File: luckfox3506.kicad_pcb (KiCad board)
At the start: 2 copper layers, 29.7 x 29.2 mm, 1 part

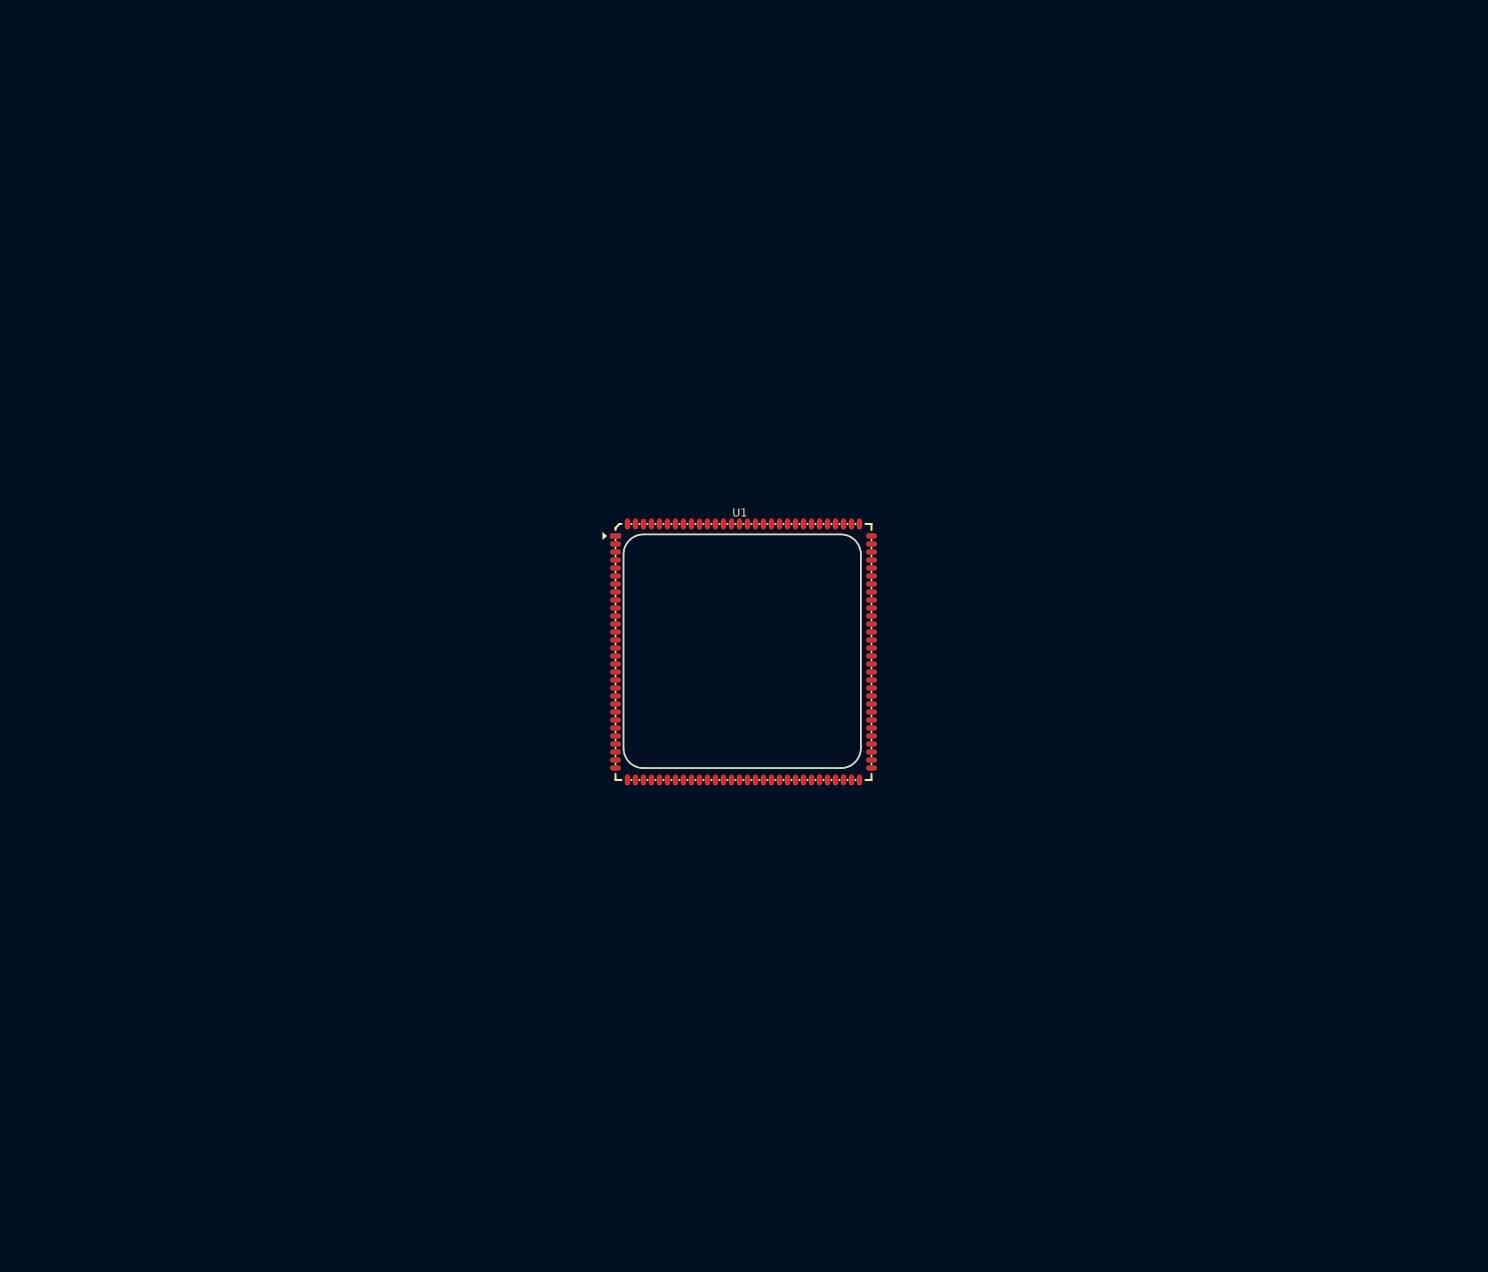
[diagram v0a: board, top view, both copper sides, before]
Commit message: Added footprints for headers
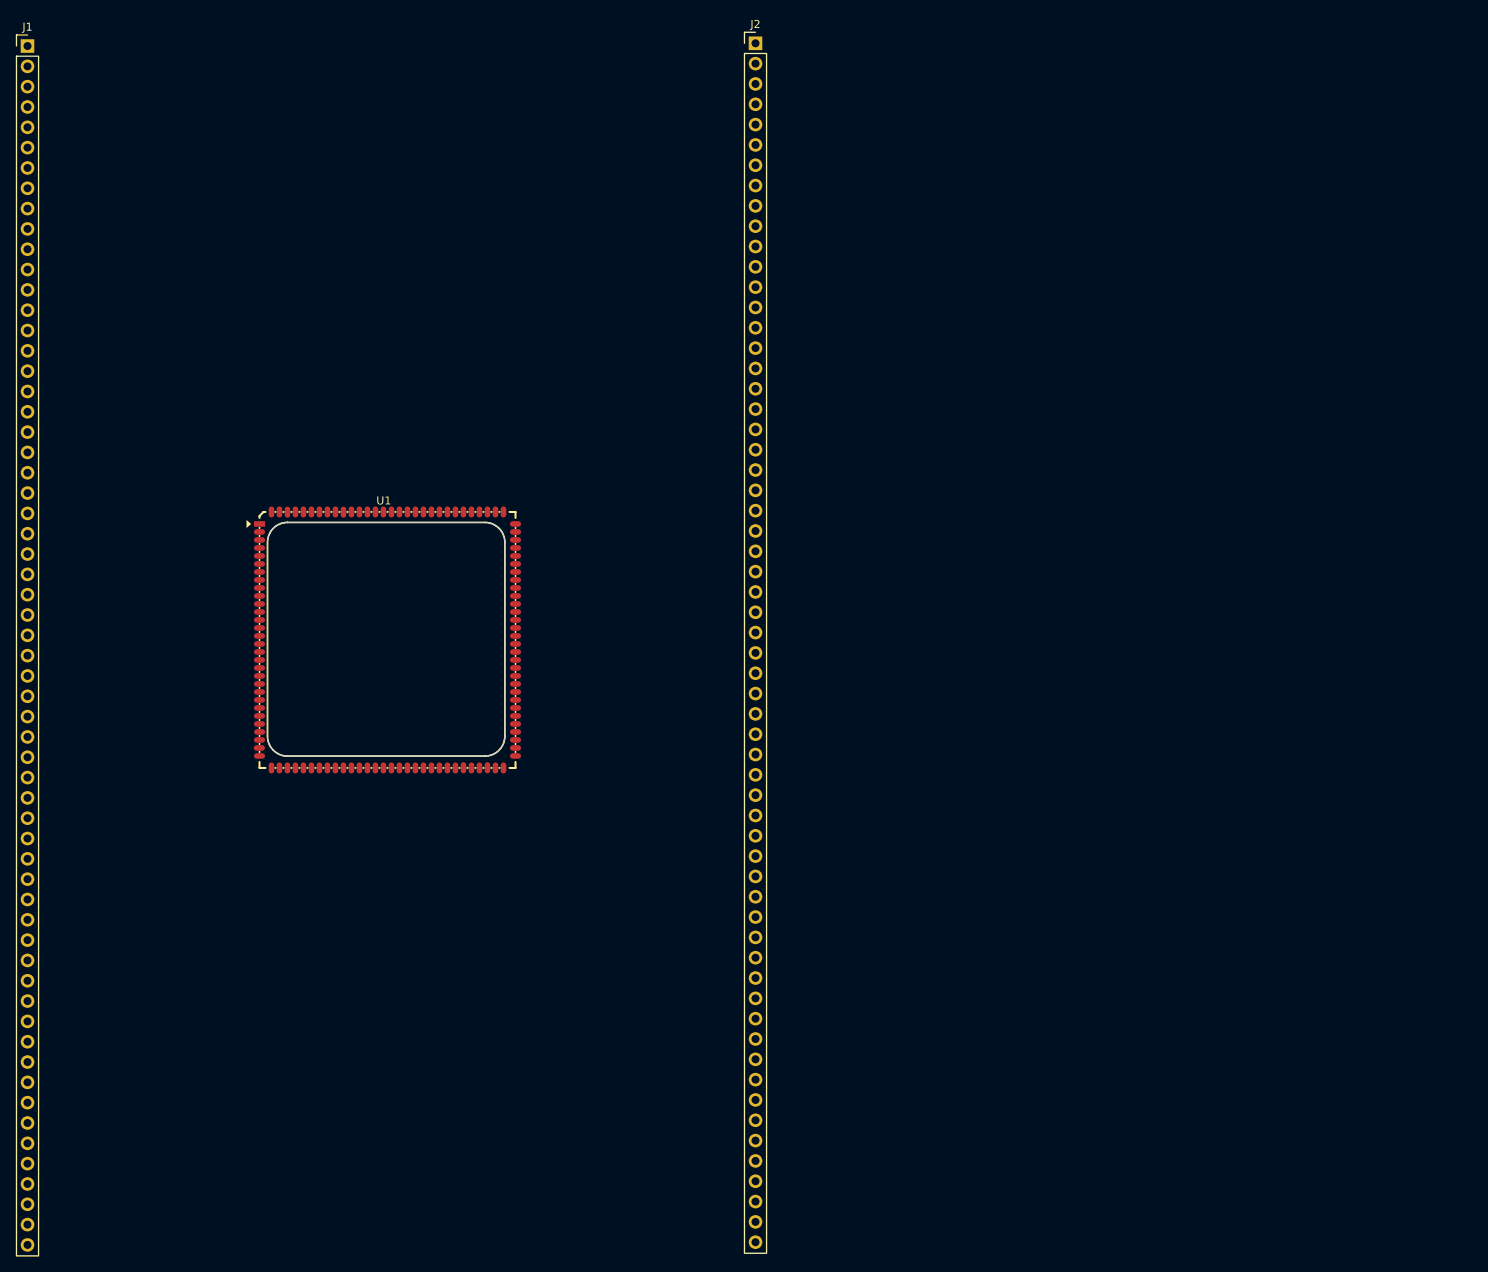
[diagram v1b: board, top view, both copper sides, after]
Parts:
- added J1: Conn_01x60, Library:PinHeader_1x60_P2.54mm_Vertical, F.Cu at (60.5, 25.3)
- added J2: Conn_01x60, Library:PinHeader_1x60_P2.54mm_Vertical, F.Cu at (151.5, 24.9)
- moved U1 44.5 mm to (105.5, 99.5)

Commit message: Added nets
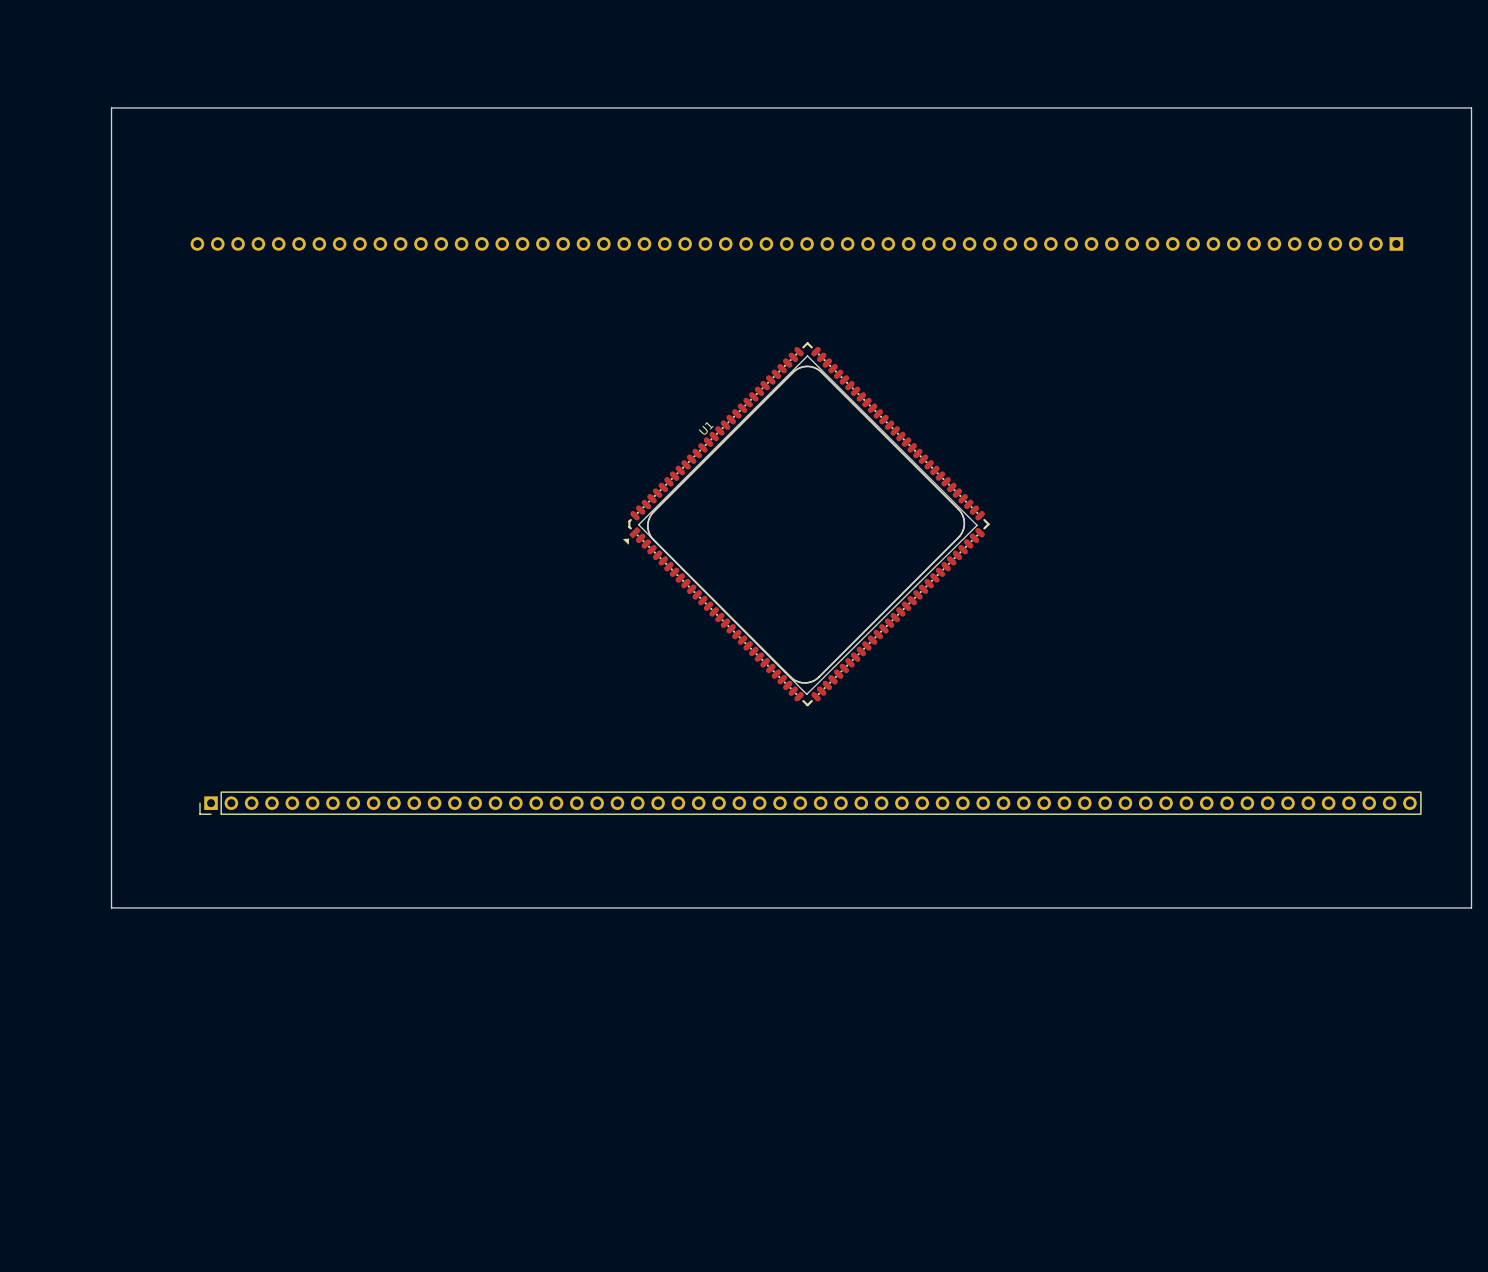
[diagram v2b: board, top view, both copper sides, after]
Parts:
- J2: moved to B.Cu
- U1: footprint Core3506:CORE3506_[32_32]_120P -> custom:CORE3506_[32_32]_120P
- moved J1 97.4 mm to (83.4, 119.9), turned to 90 degrees
- moved J2 83.9 mm to (231.6, 50.0), turned to 90 degrees
- moved U1 54.5 mm to (158.0, 85.0), turned to 45 degrees
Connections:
- J1 pad 1: unconnected-(J1-Pin_1-Pad1) -> Net-(J1-Pin_1)
- J1 pad 10: unconnected-(J1-Pin_10-Pad10) -> Net-(J1-Pin_10)
- J1 pad 11: unconnected-(J1-Pin_11-Pad11) -> Net-(J1-Pin_11)
- J1 pad 12: unconnected-(J1-Pin_12-Pad12) -> Net-(J1-Pin_12)
- J1 pad 13: unconnected-(J1-Pin_13-Pad13) -> Net-(J1-Pin_13)
- J1 pad 14: unconnected-(J1-Pin_14-Pad14) -> Net-(J1-Pin_14)
- J1 pad 15: unconnected-(J1-Pin_15-Pad15) -> Net-(J1-Pin_15)
- J1 pad 16: unconnected-(J1-Pin_16-Pad16) -> Net-(J1-Pin_16)
- J1 pad 17: unconnected-(J1-Pin_17-Pad17) -> Net-(J1-Pin_17)
- J1 pad 18: unconnected-(J1-Pin_18-Pad18) -> Net-(J1-Pin_18)
- J1 pad 19: unconnected-(J1-Pin_19-Pad19) -> Net-(J1-Pin_19)
- J1 pad 2: unconnected-(J1-Pin_2-Pad2) -> Net-(J1-Pin_2)
- J1 pad 20: unconnected-(J1-Pin_20-Pad20) -> Net-(J1-Pin_20)
- J1 pad 21: unconnected-(J1-Pin_21-Pad21) -> Net-(J1-Pin_21)
- J1 pad 22: unconnected-(J1-Pin_22-Pad22) -> Net-(J1-Pin_22)
- J1 pad 23: unconnected-(J1-Pin_23-Pad23) -> Net-(J1-Pin_23)
- J1 pad 24: unconnected-(J1-Pin_24-Pad24) -> Net-(J1-Pin_24)
- J1 pad 25: unconnected-(J1-Pin_25-Pad25) -> Net-(J1-Pin_25)
- J1 pad 26: unconnected-(J1-Pin_26-Pad26) -> Net-(J1-Pin_26)
- J1 pad 27: unconnected-(J1-Pin_27-Pad27) -> Net-(J1-Pin_27)
- J1 pad 28: unconnected-(J1-Pin_28-Pad28) -> Net-(J1-Pin_28)
- J1 pad 29: unconnected-(J1-Pin_29-Pad29) -> Net-(J1-Pin_29)
- J1 pad 3: unconnected-(J1-Pin_3-Pad3) -> Net-(J1-Pin_3)
- J1 pad 30: unconnected-(J1-Pin_30-Pad30) -> Net-(J1-Pin_30)
- J1 pad 31: unconnected-(J1-Pin_31-Pad31) -> Net-(J1-Pin_31)
- J1 pad 32: unconnected-(J1-Pin_32-Pad32) -> Net-(J1-Pin_32)
- J1 pad 33: unconnected-(J1-Pin_33-Pad33) -> Net-(J1-Pin_33)
- J1 pad 34: unconnected-(J1-Pin_34-Pad34) -> Net-(J1-Pin_34)
- J1 pad 35: unconnected-(J1-Pin_35-Pad35) -> Net-(J1-Pin_35)
- J1 pad 36: unconnected-(J1-Pin_36-Pad36) -> Net-(J1-Pin_36)
- J1 pad 37: unconnected-(J1-Pin_37-Pad37) -> Net-(J1-Pin_37)
- J1 pad 38: unconnected-(J1-Pin_38-Pad38) -> Net-(J1-Pin_38)
- J1 pad 39: unconnected-(J1-Pin_39-Pad39) -> Net-(J1-Pin_39)
- J1 pad 4: unconnected-(J1-Pin_4-Pad4) -> Net-(J1-Pin_4)
- J1 pad 40: unconnected-(J1-Pin_40-Pad40) -> Net-(J1-Pin_40)
- J1 pad 41: unconnected-(J1-Pin_41-Pad41) -> Net-(J1-Pin_41)
- J1 pad 42: unconnected-(J1-Pin_42-Pad42) -> Net-(J1-Pin_42)
- J1 pad 43: unconnected-(J1-Pin_43-Pad43) -> Net-(J1-Pin_43)
- J1 pad 44: unconnected-(J1-Pin_44-Pad44) -> Net-(J1-Pin_44)
- J1 pad 45: unconnected-(J1-Pin_45-Pad45) -> Net-(J1-Pin_45)
- J1 pad 46: unconnected-(J1-Pin_46-Pad46) -> Net-(J1-Pin_46)
- J1 pad 47: unconnected-(J1-Pin_47-Pad47) -> Net-(J1-Pin_47)
- J1 pad 48: unconnected-(J1-Pin_48-Pad48) -> Net-(J1-Pin_48)
- J1 pad 49: unconnected-(J1-Pin_49-Pad49) -> Net-(J1-Pin_49)
- J1 pad 5: unconnected-(J1-Pin_5-Pad5) -> Net-(J1-Pin_5)
- J1 pad 50: unconnected-(J1-Pin_50-Pad50) -> Net-(J1-Pin_50)
- J1 pad 51: unconnected-(J1-Pin_51-Pad51) -> Net-(J1-Pin_51)
- J1 pad 52: unconnected-(J1-Pin_52-Pad52) -> Net-(J1-Pin_52)
- J1 pad 53: unconnected-(J1-Pin_53-Pad53) -> Net-(J1-Pin_53)
- J1 pad 54: unconnected-(J1-Pin_54-Pad54) -> Net-(J1-Pin_54)
- J1 pad 55: unconnected-(J1-Pin_55-Pad55) -> Net-(J1-Pin_55)
- J1 pad 56: unconnected-(J1-Pin_56-Pad56) -> Net-(J1-Pin_56)
- J1 pad 57: unconnected-(J1-Pin_57-Pad57) -> Net-(J1-Pin_57)
- J1 pad 58: unconnected-(J1-Pin_58-Pad58) -> Net-(J1-Pin_58)
- J1 pad 59: unconnected-(J1-Pin_59-Pad59) -> Net-(J1-Pin_59)
- J1 pad 6: unconnected-(J1-Pin_6-Pad6) -> Net-(J1-Pin_6)
- J1 pad 60: unconnected-(J1-Pin_60-Pad60) -> Net-(J1-Pin_60)
- J1 pad 7: unconnected-(J1-Pin_7-Pad7) -> Net-(J1-Pin_7)
- J1 pad 8: unconnected-(J1-Pin_8-Pad8) -> Net-(J1-Pin_8)
- J1 pad 9: unconnected-(J1-Pin_9-Pad9) -> Net-(J1-Pin_9)
- J2 pad 1: unconnected-(J2-Pin_1-Pad1) -> Net-(J2-Pin_1)
- J2 pad 10: unconnected-(J2-Pin_10-Pad10) -> Net-(J2-Pin_10)
- J2 pad 11: unconnected-(J2-Pin_11-Pad11) -> Net-(J2-Pin_11)
- J2 pad 12: unconnected-(J2-Pin_12-Pad12) -> Net-(J2-Pin_12)
- J2 pad 13: unconnected-(J2-Pin_13-Pad13) -> Net-(J2-Pin_13)
- J2 pad 14: unconnected-(J2-Pin_14-Pad14) -> Net-(J2-Pin_14)
- J2 pad 15: unconnected-(J2-Pin_15-Pad15) -> Net-(J2-Pin_15)
- J2 pad 16: unconnected-(J2-Pin_16-Pad16) -> Net-(J2-Pin_16)
- J2 pad 17: unconnected-(J2-Pin_17-Pad17) -> Net-(J2-Pin_17)
- J2 pad 18: unconnected-(J2-Pin_18-Pad18) -> Net-(J2-Pin_18)
- J2 pad 19: unconnected-(J2-Pin_19-Pad19) -> Net-(J2-Pin_19)
- J2 pad 2: unconnected-(J2-Pin_2-Pad2) -> Net-(J2-Pin_2)
- J2 pad 20: unconnected-(J2-Pin_20-Pad20) -> Net-(J2-Pin_20)
- J2 pad 21: unconnected-(J2-Pin_21-Pad21) -> Net-(J2-Pin_21)
- J2 pad 22: unconnected-(J2-Pin_22-Pad22) -> Net-(J2-Pin_22)
- J2 pad 23: unconnected-(J2-Pin_23-Pad23) -> Net-(J2-Pin_23)
- J2 pad 24: unconnected-(J2-Pin_24-Pad24) -> Net-(J2-Pin_24)
- J2 pad 25: unconnected-(J2-Pin_25-Pad25) -> Net-(J2-Pin_25)
- J2 pad 26: unconnected-(J2-Pin_26-Pad26) -> Net-(J2-Pin_26)
- J2 pad 27: unconnected-(J2-Pin_27-Pad27) -> Net-(J2-Pin_27)
- J2 pad 28: unconnected-(J2-Pin_28-Pad28) -> Net-(J2-Pin_28)
- J2 pad 29: unconnected-(J2-Pin_29-Pad29) -> Net-(J2-Pin_29)
- J2 pad 3: unconnected-(J2-Pin_3-Pad3) -> Net-(J2-Pin_3)
- J2 pad 30: unconnected-(J2-Pin_30-Pad30) -> Net-(J2-Pin_30)
- J2 pad 31: unconnected-(J2-Pin_31-Pad31) -> Net-(J2-Pin_31)
- J2 pad 32: unconnected-(J2-Pin_32-Pad32) -> Net-(J2-Pin_32)
- J2 pad 33: unconnected-(J2-Pin_33-Pad33) -> Net-(J2-Pin_33)
- J2 pad 34: unconnected-(J2-Pin_34-Pad34) -> Net-(J2-Pin_34)
- J2 pad 35: unconnected-(J2-Pin_35-Pad35) -> Net-(J2-Pin_35)
- J2 pad 36: unconnected-(J2-Pin_36-Pad36) -> Net-(J2-Pin_36)
- J2 pad 37: unconnected-(J2-Pin_37-Pad37) -> Net-(J2-Pin_37)
- J2 pad 38: unconnected-(J2-Pin_38-Pad38) -> Net-(J2-Pin_38)
- J2 pad 39: unconnected-(J2-Pin_39-Pad39) -> Net-(J2-Pin_39)
- J2 pad 4: unconnected-(J2-Pin_4-Pad4) -> Net-(J2-Pin_4)
- J2 pad 40: unconnected-(J2-Pin_40-Pad40) -> Net-(J2-Pin_40)
- J2 pad 41: unconnected-(J2-Pin_41-Pad41) -> Net-(J2-Pin_41)
- J2 pad 42: unconnected-(J2-Pin_42-Pad42) -> Net-(J2-Pin_42)
- J2 pad 43: unconnected-(J2-Pin_43-Pad43) -> Net-(J2-Pin_43)
- J2 pad 44: unconnected-(J2-Pin_44-Pad44) -> Net-(J2-Pin_44)
- J2 pad 45: unconnected-(J2-Pin_45-Pad45) -> Net-(J2-Pin_45)
- J2 pad 46: unconnected-(J2-Pin_46-Pad46) -> Net-(J2-Pin_46)
- J2 pad 47: unconnected-(J2-Pin_47-Pad47) -> Net-(J2-Pin_47)
- J2 pad 48: unconnected-(J2-Pin_48-Pad48) -> Net-(J2-Pin_48)
- J2 pad 49: unconnected-(J2-Pin_49-Pad49) -> Net-(J2-Pin_49)
- J2 pad 5: unconnected-(J2-Pin_5-Pad5) -> Net-(J2-Pin_5)
- J2 pad 50: unconnected-(J2-Pin_50-Pad50) -> Net-(J2-Pin_50)
- J2 pad 51: unconnected-(J2-Pin_51-Pad51) -> Net-(J2-Pin_51)
- J2 pad 52: unconnected-(J2-Pin_52-Pad52) -> Net-(J2-Pin_52)
- J2 pad 53: unconnected-(J2-Pin_53-Pad53) -> Net-(J2-Pin_53)
- J2 pad 54: unconnected-(J2-Pin_54-Pad54) -> Net-(J2-Pin_54)
- J2 pad 55: unconnected-(J2-Pin_55-Pad55) -> Net-(J2-Pin_55)
- J2 pad 56: unconnected-(J2-Pin_56-Pad56) -> Net-(J2-Pin_56)
- J2 pad 57: unconnected-(J2-Pin_57-Pad57) -> Net-(J2-Pin_57)
- J2 pad 58: unconnected-(J2-Pin_58-Pad58) -> Net-(J2-Pin_58)
- J2 pad 59: unconnected-(J2-Pin_59-Pad59) -> Net-(J2-Pin_59)
- J2 pad 6: unconnected-(J2-Pin_6-Pad6) -> Net-(J2-Pin_6)
- J2 pad 60: unconnected-(J2-Pin_60-Pad60) -> Net-(J2-Pin_60)
- J2 pad 7: unconnected-(J2-Pin_7-Pad7) -> Net-(J2-Pin_7)
- J2 pad 8: unconnected-(J2-Pin_8-Pad8) -> Net-(J2-Pin_8)
- J2 pad 9: unconnected-(J2-Pin_9-Pad9) -> Net-(J2-Pin_9)
- U1 pad 1: (no net) -> Net-(J1-Pin_1)
- U1 pad 10: (no net) -> Net-(J1-Pin_10)
- U1 pad 100: (no net) -> Net-(J2-Pin_40)
- U1 pad 101: (no net) -> Net-(J2-Pin_41)
- U1 pad 102: (no net) -> Net-(J2-Pin_42)
- U1 pad 103: (no net) -> Net-(J2-Pin_43)
- U1 pad 104: (no net) -> Net-(J2-Pin_44)
- U1 pad 105: (no net) -> Net-(J2-Pin_45)
- U1 pad 106: (no net) -> Net-(J2-Pin_46)
- U1 pad 107: (no net) -> Net-(J2-Pin_47)
- U1 pad 108: (no net) -> Net-(J2-Pin_48)
- U1 pad 109: (no net) -> Net-(J2-Pin_49)
- U1 pad 11: (no net) -> Net-(J1-Pin_11)
- U1 pad 110: (no net) -> Net-(J2-Pin_50)
- U1 pad 111: (no net) -> Net-(J2-Pin_51)
- U1 pad 112: (no net) -> Net-(J2-Pin_52)
- U1 pad 113: (no net) -> Net-(J2-Pin_53)
- U1 pad 114: (no net) -> Net-(J2-Pin_54)
- U1 pad 115: (no net) -> Net-(J2-Pin_55)
- U1 pad 116: (no net) -> Net-(J2-Pin_56)
- U1 pad 117: (no net) -> Net-(J2-Pin_57)
- U1 pad 118: (no net) -> Net-(J2-Pin_58)
- U1 pad 119: (no net) -> Net-(J2-Pin_59)
- U1 pad 12: (no net) -> Net-(J1-Pin_12)
- U1 pad 120: (no net) -> Net-(J2-Pin_60)
- U1 pad 13: (no net) -> Net-(J1-Pin_13)
- U1 pad 14: (no net) -> Net-(J1-Pin_14)
- U1 pad 15: (no net) -> Net-(J1-Pin_15)
- U1 pad 16: (no net) -> Net-(J1-Pin_16)
- U1 pad 17: (no net) -> Net-(J1-Pin_17)
- U1 pad 18: (no net) -> Net-(J1-Pin_18)
- U1 pad 19: (no net) -> Net-(J1-Pin_19)
- U1 pad 2: (no net) -> Net-(J1-Pin_2)
- U1 pad 20: (no net) -> Net-(J1-Pin_20)
- U1 pad 21: (no net) -> Net-(J1-Pin_21)
- U1 pad 22: (no net) -> Net-(J1-Pin_22)
- U1 pad 23: (no net) -> Net-(J1-Pin_23)
- U1 pad 24: (no net) -> Net-(J1-Pin_24)
- U1 pad 25: (no net) -> Net-(J1-Pin_25)
- U1 pad 26: (no net) -> Net-(J1-Pin_26)
- U1 pad 27: (no net) -> Net-(J1-Pin_27)
- U1 pad 28: (no net) -> Net-(J1-Pin_28)
- U1 pad 29: (no net) -> Net-(J1-Pin_29)
- U1 pad 3: (no net) -> Net-(J1-Pin_3)
- U1 pad 30: (no net) -> Net-(J1-Pin_30)
- U1 pad 31: (no net) -> Net-(J1-Pin_31)
- U1 pad 32: (no net) -> Net-(J1-Pin_32)
- U1 pad 33: (no net) -> Net-(J1-Pin_33)
- U1 pad 34: (no net) -> Net-(J1-Pin_34)
- U1 pad 35: (no net) -> Net-(J1-Pin_35)
- U1 pad 36: (no net) -> Net-(J1-Pin_36)
- U1 pad 37: (no net) -> Net-(J1-Pin_37)
- U1 pad 38: (no net) -> Net-(J1-Pin_38)
- U1 pad 39: (no net) -> Net-(J1-Pin_39)
- U1 pad 4: (no net) -> Net-(J1-Pin_4)
- U1 pad 40: (no net) -> Net-(J1-Pin_40)
- U1 pad 41: (no net) -> Net-(J1-Pin_41)
- U1 pad 42: (no net) -> Net-(J1-Pin_42)
- U1 pad 43: (no net) -> Net-(J1-Pin_43)
- U1 pad 44: (no net) -> Net-(J1-Pin_44)
- U1 pad 45: (no net) -> Net-(J1-Pin_45)
- U1 pad 46: (no net) -> Net-(J1-Pin_46)
- U1 pad 47: (no net) -> Net-(J1-Pin_47)
- U1 pad 48: (no net) -> Net-(J1-Pin_48)
- U1 pad 49: (no net) -> Net-(J1-Pin_49)
- U1 pad 5: (no net) -> Net-(J1-Pin_5)
- U1 pad 50: (no net) -> Net-(J1-Pin_50)
- U1 pad 51: (no net) -> Net-(J1-Pin_51)
- U1 pad 52: (no net) -> Net-(J1-Pin_52)
- U1 pad 53: (no net) -> Net-(J1-Pin_53)
- U1 pad 54: (no net) -> Net-(J1-Pin_54)
- U1 pad 55: (no net) -> Net-(J1-Pin_55)
- U1 pad 56: (no net) -> Net-(J1-Pin_56)
- U1 pad 57: (no net) -> Net-(J1-Pin_57)
- U1 pad 58: (no net) -> Net-(J1-Pin_58)
- U1 pad 59: (no net) -> Net-(J1-Pin_59)
- U1 pad 6: (no net) -> Net-(J1-Pin_6)
- U1 pad 60: (no net) -> Net-(J1-Pin_60)
- U1 pad 61: (no net) -> Net-(J2-Pin_1)
- U1 pad 62: (no net) -> Net-(J2-Pin_2)
- U1 pad 63: (no net) -> Net-(J2-Pin_3)
- U1 pad 64: (no net) -> Net-(J2-Pin_4)
- U1 pad 65: (no net) -> Net-(J2-Pin_5)
- U1 pad 66: (no net) -> Net-(J2-Pin_6)
- U1 pad 67: (no net) -> Net-(J2-Pin_7)
- U1 pad 68: (no net) -> Net-(J2-Pin_8)
- U1 pad 69: (no net) -> Net-(J2-Pin_9)
- U1 pad 7: (no net) -> Net-(J1-Pin_7)
- U1 pad 70: (no net) -> Net-(J2-Pin_10)
- U1 pad 71: (no net) -> Net-(J2-Pin_11)
- U1 pad 72: (no net) -> Net-(J2-Pin_12)
- U1 pad 73: (no net) -> Net-(J2-Pin_13)
- U1 pad 74: (no net) -> Net-(J2-Pin_14)
- U1 pad 75: (no net) -> Net-(J2-Pin_15)
- U1 pad 76: (no net) -> Net-(J2-Pin_16)
- U1 pad 77: (no net) -> Net-(J2-Pin_17)
- U1 pad 78: (no net) -> Net-(J2-Pin_18)
- U1 pad 79: (no net) -> Net-(J2-Pin_19)
- U1 pad 8: (no net) -> Net-(J1-Pin_8)
- U1 pad 80: (no net) -> Net-(J2-Pin_20)
- U1 pad 81: (no net) -> Net-(J2-Pin_21)
- U1 pad 82: (no net) -> Net-(J2-Pin_22)
- U1 pad 83: (no net) -> Net-(J2-Pin_23)
- U1 pad 84: (no net) -> Net-(J2-Pin_24)
- U1 pad 85: (no net) -> Net-(J2-Pin_25)
- U1 pad 86: (no net) -> Net-(J2-Pin_26)
- U1 pad 87: (no net) -> Net-(J2-Pin_27)
- U1 pad 88: (no net) -> Net-(J2-Pin_28)
- U1 pad 89: (no net) -> Net-(J2-Pin_29)
- U1 pad 9: (no net) -> Net-(J1-Pin_9)
- U1 pad 90: (no net) -> Net-(J2-Pin_30)
- U1 pad 91: (no net) -> Net-(J2-Pin_31)
- U1 pad 92: (no net) -> Net-(J2-Pin_32)
- U1 pad 93: (no net) -> Net-(J2-Pin_33)
- U1 pad 94: (no net) -> Net-(J2-Pin_34)
- U1 pad 95: (no net) -> Net-(J2-Pin_35)
- U1 pad 96: (no net) -> Net-(J2-Pin_36)
- U1 pad 97: (no net) -> Net-(J2-Pin_37)
- U1 pad 98: (no net) -> Net-(J2-Pin_38)
- U1 pad 99: (no net) -> Net-(J2-Pin_39)
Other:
- board size 29.7 x 29.2 mm -> 170 x 100 mm
